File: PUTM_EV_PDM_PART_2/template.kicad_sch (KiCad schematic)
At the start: 6 parts, among them J2 UPS-08-07.0-01-L-V, J3 Conn_02x18_Counter_Clockwise, J4 Conn_01x06, J5 +24V OUT, J7 UPS-08-07.0-01-L-V, J8 +24V IN

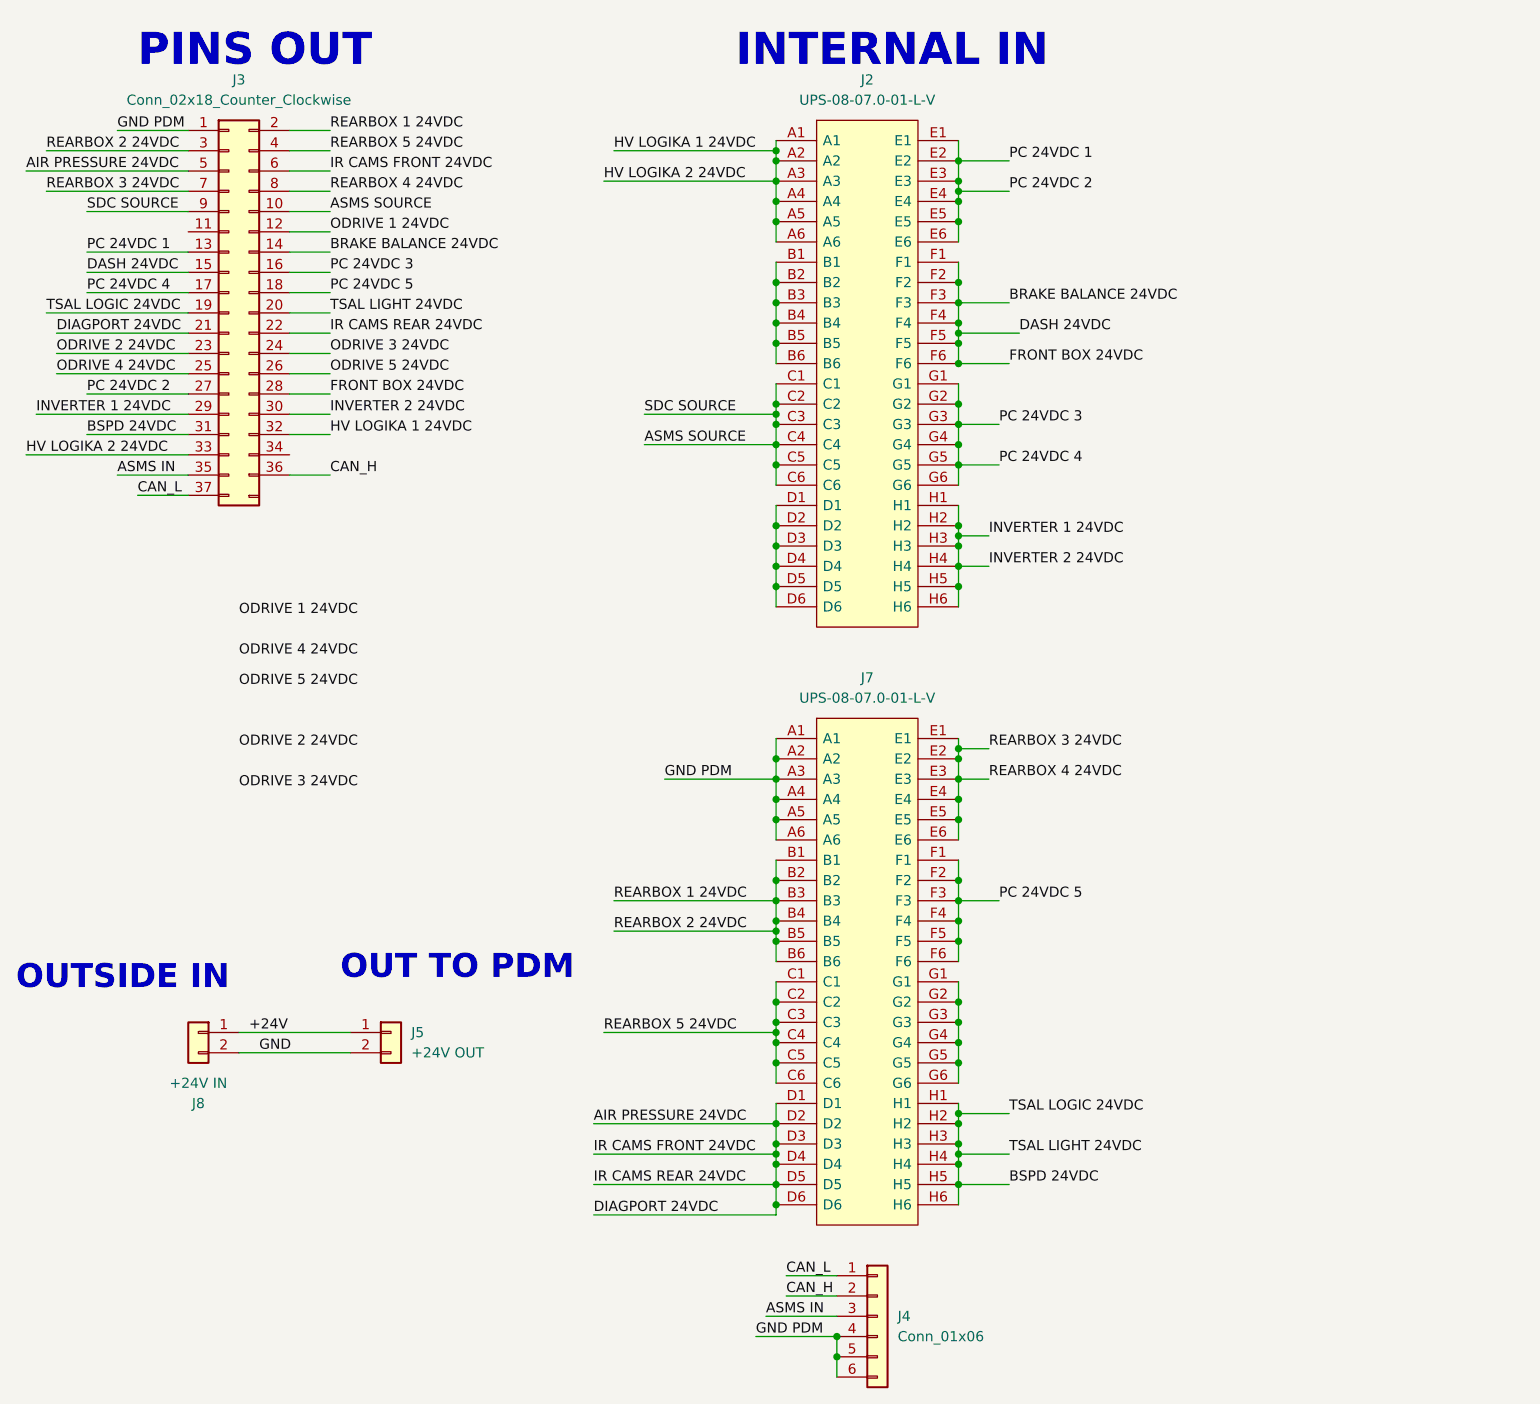
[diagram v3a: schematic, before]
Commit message: Added Fan and pump support.
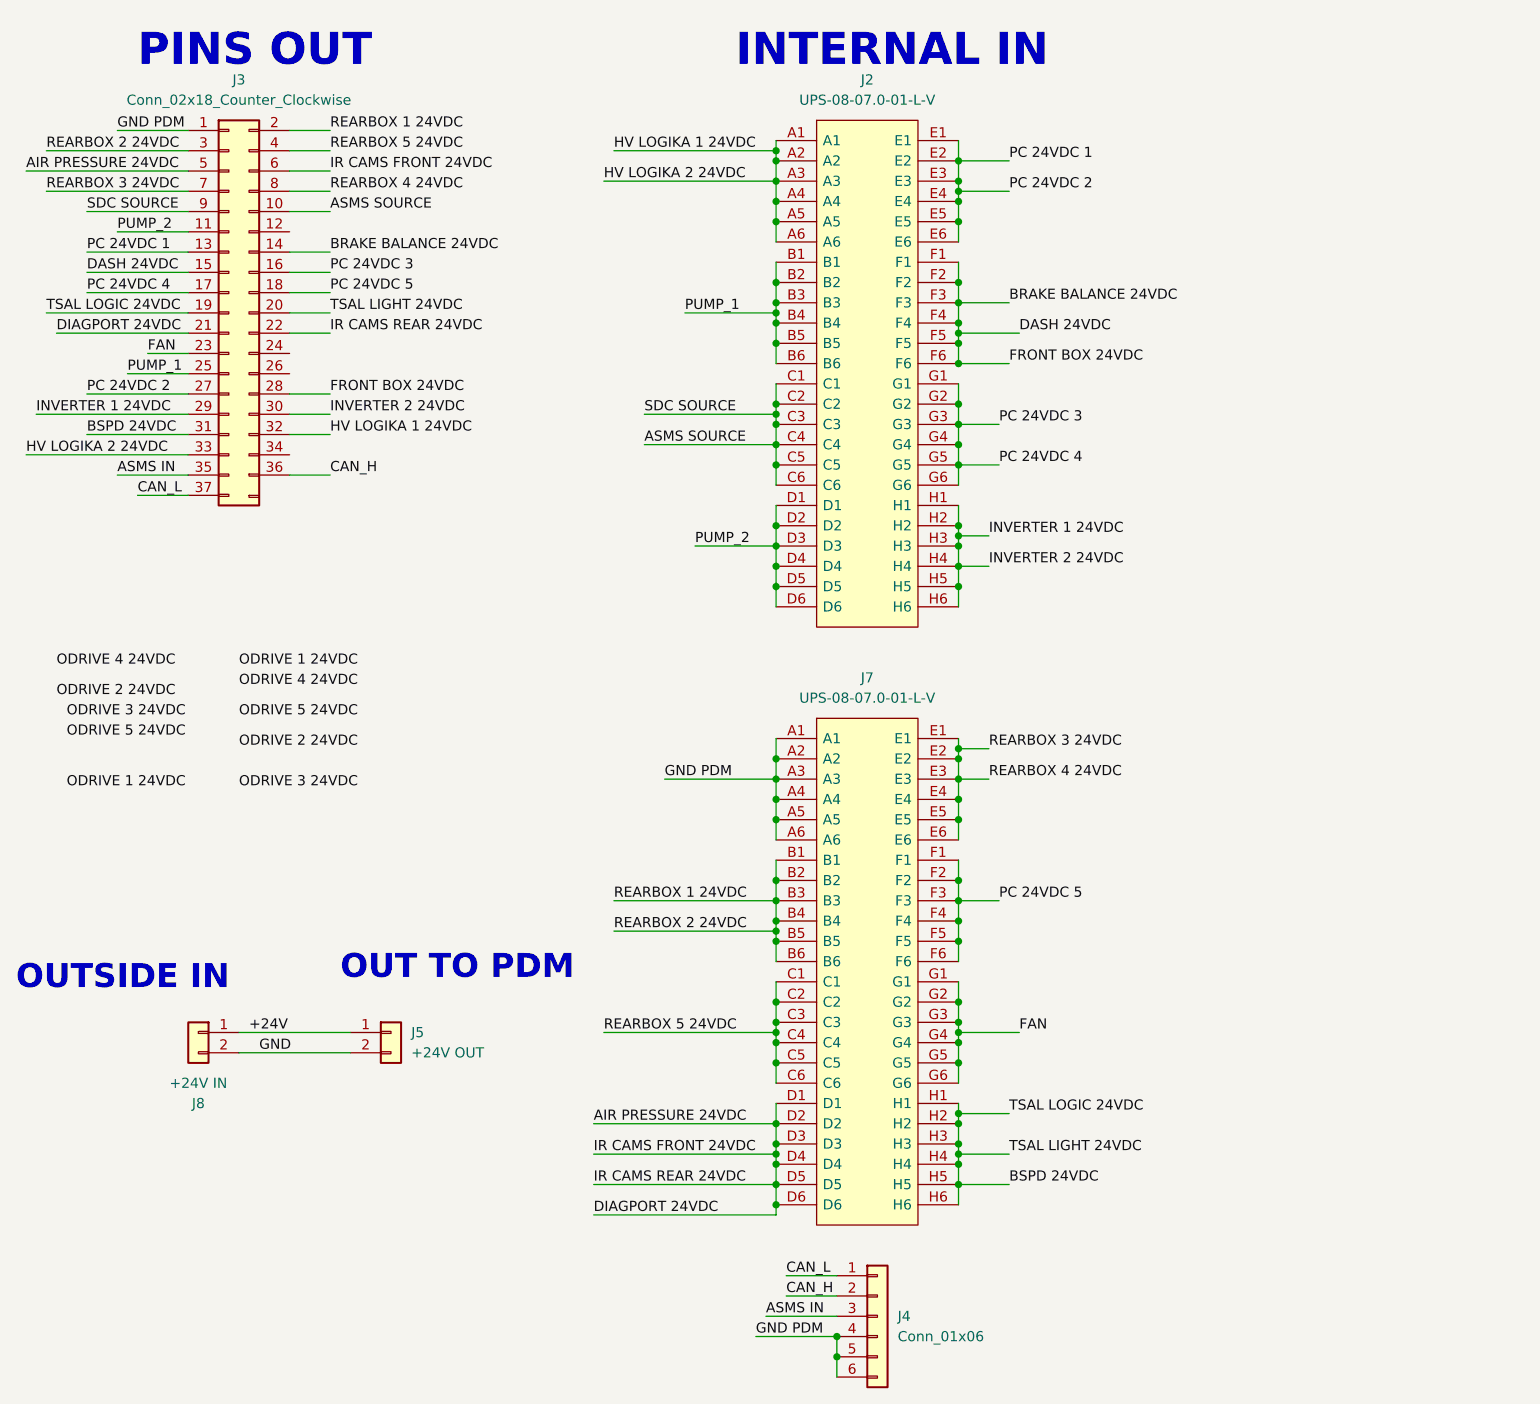
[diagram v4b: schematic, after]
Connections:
- net ODRIVE 1 24VDC: no longer J3.12 (Pin_12)
- net ODRIVE 2 24VDC: no longer J3.23 (Pin_23)
- net ODRIVE 3 24VDC: no longer J3.24 (Pin_24)
- net ODRIVE 4 24VDC: no longer J3.25 (Pin_25)
- net ODRIVE 5 24VDC: no longer J3.26 (Pin_26)
- net FAN: now reaches J7.G1, J7.G2, J7.G3, J7.G4, J7.G5, J7.G6
- net FAN: now also J3.23 (Pin_23)
- net PUMP_2: now reaches J3.11 (Pin_11)
- net PUMP_2: now also J2.D1, J2.D2, J2.D3, J2.D4, J2.D5, J2.D6
- net PUMP_1: now reaches J2.B1, J2.B2, J2.B3, J2.B4, J2.B5, J2.B6
- net PUMP_1: now also J3.25 (Pin_25)
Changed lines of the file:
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@@
   (junction (at 110.49 143.51) (diameter 0) (color 0 0 0 0)
   )
+  (junction (at 110.49 49.53) (diameter 0) (color 0 0 0 0)
+  )
   (junction (at 133.35 143.51) (diameter 0) (color 0 0 0 0)
   )
@@
   (junction (at 110.49 48.26) (diameter 0) (color 0 0 0 0)
   )
+  (junction (at 133.35 139.7) (diameter 0) (color 0 0 0 0)
+  )
   (junction (at 110.49 113.03) (diameter 0) (color 0 0 0 0)
   )
@@
     (stroke (width 0) (type default))
   )
-  (wire (pts (xy 49.53 54.61) (xy 54.61 54.61))
-    (stroke (width 0) (type default))
-  )
   (wire (pts (xy 110.49 62.23) (xy 110.49 63.5))
     (stroke (width 0) (type default))
@@
     (stroke (width 0) (type default))
   )
+  (wire (pts (xy 100.33 78.74) (xy 110.49 78.74))
+    (stroke (width 0) (type default))
+  )
   (wire (pts (xy 110.49 140.97) (xy 110.49 143.51))
     (stroke (width 0) (type default))
@@
     (stroke (width 0) (type default))
   )
-  (wire (pts (xy 20.32 57.15) (xy 36.83 57.15))
+  (wire (pts (xy 133.35 139.7) (xy 140.97 139.7))
     (stroke (width 0) (type default))
   )
@@
     (stroke (width 0) (type default))
   )
+  (wire (pts (xy 99.06 49.53) (xy 110.49 49.53))
+    (stroke (width 0) (type default))
+  )
   (wire (pts (xy 24.13 41.91) (xy 36.83 41.91))
     (stroke (width 0) (type default))
@@
     (stroke (width 0) (type default))
   )
+  (wire (pts (xy 29.21 57.15) (xy 36.83 57.15))
+    (stroke (width 0) (type default))
+  )
   (wire (pts (xy 110.49 143.51) (xy 110.49 146.05))
     (stroke (width 0) (type default))
@@
     (stroke (width 0) (type default))
   )
-  (wire (pts (xy 49.53 39.37) (xy 54.61 39.37))
-    (stroke (width 0) (type default))
-  )
   (wire (pts (xy 49.53 26.67) (xy 54.61 26.67))
     (stroke (width 0) (type default))
@@
     (stroke (width 0) (type default))
   )
-  (wire (pts (xy 20.32 54.61) (xy 36.83 54.61))
-    (stroke (width 0) (type default))
-  )
   (wire (pts (xy 27.94 69.85) (xy 36.83 69.85))
     (stroke (width 0) (type default))
@@
     (stroke (width 0) (type default))
   )
+  (wire (pts (xy 27.94 39.37) (xy 36.83 39.37))
+    (stroke (width 0) (type default))
+  )
   (wire (pts (xy 87.63 151.13) (xy 110.49 151.13))
     (stroke (width 0) (type default))
@@
     (stroke (width 0) (type default))
   )
-  (wire (pts (xy 49.53 57.15) (xy 54.61 57.15))
-    (stroke (width 0) (type default))
-  )
   (wire (pts (xy 88.9 139.7) (xy 110.49 139.7))
     (stroke (width 0) (type default))
@@
     (stroke (width 0) (type default))
   )
+  (wire (pts (xy 31.75 54.61) (xy 36.83 54.61))
+    (stroke (width 0) (type default))
+  )
   (wire (pts (xy 133.35 52.07) (xy 133.35 53.34))
     (stroke (width 0) (type default))
@@
     (stroke (width 0) (type default))
   )
+  (wire (pts (xy 110.49 49.53) (xy 110.49 50.8))
+    (stroke (width 0) (type default))
+  )
   (wire (pts (xy 110.49 58.42) (xy 110.49 60.96))
     (stroke (width 0) (type default))
@@
     (stroke (width 0) (type default))
   )
-  (wire (pts (xy 110.49 48.26) (xy 110.49 50.8))
+  (wire (pts (xy 110.49 48.26) (xy 110.49 49.53))
     (stroke (width 0) (type default))
   )
@@
     (stroke (width 0) (type default))
   )
+  (wire (pts (xy 133.35 139.7) (xy 133.35 140.97))
+    (stroke (width 0) (type default))
+  )
   (wire (pts (xy 87.63 154.94) (xy 110.49 154.94))
     (stroke (width 0) (type default))
@@
     (stroke (width 0) (type default))
   )
-  (wire (pts (xy 133.35 138.43) (xy 133.35 140.97))
+  (wire (pts (xy 133.35 138.43) (xy 133.35 139.7))
     (stroke (width 0) (type default))
   )
@@
     (effects (font (size 1.27 1.27)) (justify left bottom))
   )
+  (label "PUMP_2" (at 27.94 39.37 0) (fields_autoplaced)
+    (effects (font (size 1.27 1.27)) (justify left bottom))
+  )
   (label "AIR PRESSURE 24VDC" (at 87.63 151.13 0) (fields_autoplaced)
     (effects (font (size 1.27 1.27)) (justify left bottom))
@@
     (effects (font (size 1.27 1.27)) (justify left bottom))
   )
-  (label "ODRIVE 5 24VDC" (at 43.18 96.52 0) (fields_autoplaced)
+  (label "ODRIVE 5 24VDC" (at 43.18 100.33 0) (fields_autoplaced)
     (effects (font (size 1.27 1.27)) (justify left bottom))
   )
@@
     (effects (font (size 1.27 1.27)) (justify left bottom))
   )
+  (label "PUMP_1" (at 99.06 49.53 0) (fields_autoplaced)
+    (effects (font (size 1.27 1.27)) (justify left bottom))
+  )
   (label "PC 24VDC 5" (at 138.43 123.19 0) (fields_autoplaced)
     (effects (font (size 1.27 1.27)) (justify left bottom))
@@
     (effects (font (size 1.27 1.27)) (justify left bottom))
   )
-  (label "ODRIVE 1 24VDC" (at 54.61 39.37 0) (fields_autoplaced)
+  (label "ODRIVE 1 24VDC" (at 21.59 109.22 0) (fields_autoplaced)
     (effects (font (size 1.27 1.27)) (justify left bottom))
   )
@@
     (effects (font (size 1.27 1.27)) (justify left bottom))
   )
-  (label "ODRIVE 4 24VDC" (at 43.18 92.71 0) (fields_autoplaced)
+  (label "ODRIVE 4 24VDC" (at 43.18 96.52 0) (fields_autoplaced)
     (effects (font (size 1.27 1.27)) (justify left bottom))
   )
@@
     (effects (font (size 1.27 1.27)) (justify left bottom))
   )
-  (label "ODRIVE 1 24VDC" (at 43.18 87.63 0) (fields_autoplaced)
+  (label "ODRIVE 1 24VDC" (at 43.18 93.98 0) (fields_autoplaced)
     (effects (font (size 1.27 1.27)) (justify left bottom))
   )
@@
     (effects (font (size 1.27 1.27)) (justify left bottom))
   )
-  (label "ODRIVE 4 24VDC" (at 20.32 57.15 0) (fields_autoplaced)
+  (label "ODRIVE 4 24VDC" (at 20.32 93.98 0) (fields_autoplaced)
     (effects (font (size 1.27 1.27)) (justify left bottom))
   )
@@
     (effects (font (size 1.27 1.27)) (justify left bottom))
   )
+  (label "PUMP_1" (at 29.21 57.15 0) (fields_autoplaced)
+    (effects (font (size 1.27 1.27)) (justify left bottom))
+  )
   (label "REARBOX 1 24VDC" (at 54.61 26.67 0) (fields_autoplaced)
     (effects (font (size 1.27 1.27)) (justify left bottom))
@@
     (effects (font (size 1.27 1.27)) (justify left bottom))
   )
-  (label "ODRIVE 5 24VDC" (at 54.61 57.15 0) (fields_autoplaced)
+  (label "ODRIVE 5 24VDC" (at 21.59 102.87 0) (fields_autoplaced)
     (effects (font (size 1.27 1.27)) (justify left bottom))
   )
@@
     (effects (font (size 1.27 1.27)) (justify left bottom))
   )
-  (label "ODRIVE 2 24VDC" (at 20.32 54.61 0) (fields_autoplaced)
+  (label "FAN" (at 31.75 54.61 0) (fields_autoplaced)
+    (effects (font (size 1.27 1.27)) (justify left bottom))
+  )
+  (label "ODRIVE 2 24VDC" (at 20.32 97.79 0) (fields_autoplaced)
     (effects (font (size 1.27 1.27)) (justify left bottom))
   )
@@
     (effects (font (size 1.27 1.27)) (justify left bottom))
   )
-  (label "ODRIVE 3 24VDC" (at 54.61 54.61 0) (fields_autoplaced)
+  (label "ODRIVE 3 24VDC" (at 21.59 100.33 0) (fields_autoplaced)
+    (effects (font (size 1.27 1.27)) (justify left bottom))
+  )
+  (label "PUMP_2" (at 100.33 78.74 0) (fields_autoplaced)
     (effects (font (size 1.27 1.27)) (justify left bottom))
   )
@@
     (effects (font (size 1.27 1.27)) (justify left bottom))
   )
+  (label "FAN" (at 140.97 139.7 0) (fields_autoplaced)
+    (effects (font (size 1.27 1.27)) (justify left bottom))
+  )

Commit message: Add files via upload
Fixed fan and pump routing, fixed spacing between internal connectors to fit PDM
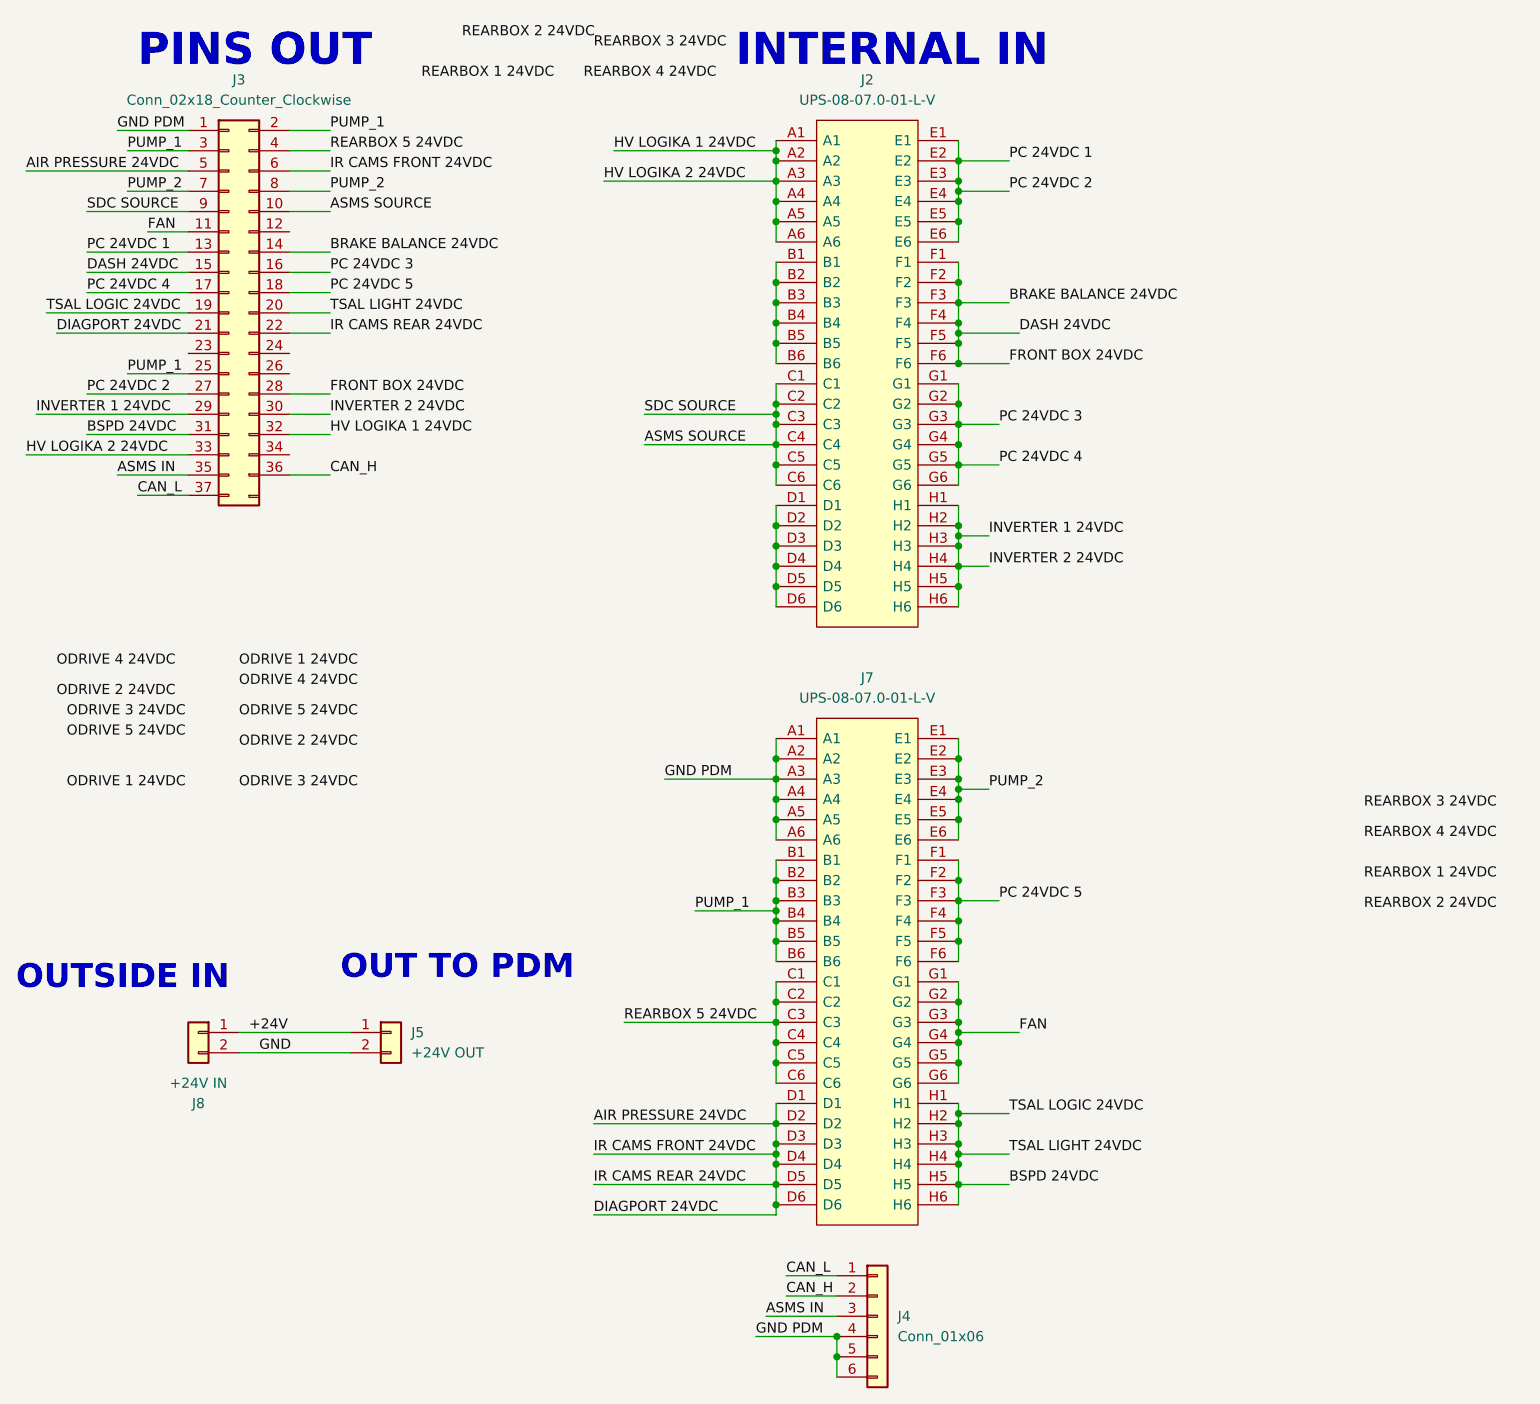
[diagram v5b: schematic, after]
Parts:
- J5: footprint UPS-02-04.0-01-L-V:SAMTEC_UPS-02-04.0-01-L-V -> UPS-02-07.0-01-L-V:SAMTEC_UPS-02-XX.X-X-X-V
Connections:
- net FAN: now also J3.11 (Pin_11); no longer J3.23 (Pin_23)
- net PUMP_1: now also J3.2 (Pin_2), J3.3 (Pin_3), J7.B1, J7.B2, J7.B3, J7.B4, J7.B5, J7.B6; no longer J2.B1, J2.B2, J2.B3, J2.B4, J2.B5, J2.B6
- net PUMP_2: now also J3.7 (Pin_7), J3.8 (Pin_8), J7.E1, J7.E2, J7.E3, J7.E4, J7.E5, J7.E6; no longer J2.D1, J2.D2, J2.D3, J2.D4, J2.D5, J2.D6, J3.11 (Pin_11)
- net REARBOX 1 24VDC: no longer J3.2 (Pin_2), J3.3 (Pin_3), J7.B1, J7.B2, J7.B3, J7.B4, J7.B5, J7.B6
- net REARBOX 3 24VDC: no longer J3.7 (Pin_7), J3.8 (Pin_8), J7.E1, J7.E2, J7.E3, J7.E4, J7.E5, J7.E6
- new net: J2.B1, J2.B2, J2.B3, J2.B4, J2.B5, J2.B6
- new net: J2.D1, J2.D2, J2.D3, J2.D4, J2.D5, J2.D6
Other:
- company: Author: -> Author: Wiktor Krakowski 
